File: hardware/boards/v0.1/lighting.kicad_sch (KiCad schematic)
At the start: 19 parts, among them U10 TRIG9, U11 TRIG13, U12 TRIG10, U13 TRIG14, U14 TRIG11, U15 TRIG15, U16 TRIG12, U17 TRIG16, U2 TRIG1, U3 TRIG2, U33 SN74AHCT1G125DBVR, U4 TRIG3, U5 TRIG4, U6 TRIG8, U7 TRIG7, U8 TRIG6, U9 TRIG5

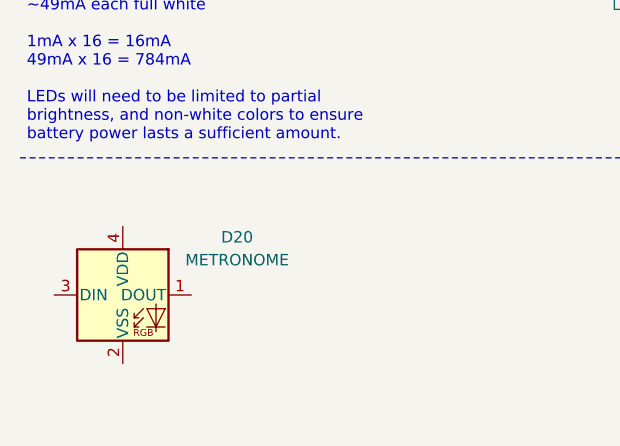
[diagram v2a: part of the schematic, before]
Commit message: feat: more routing and DRC cleanup
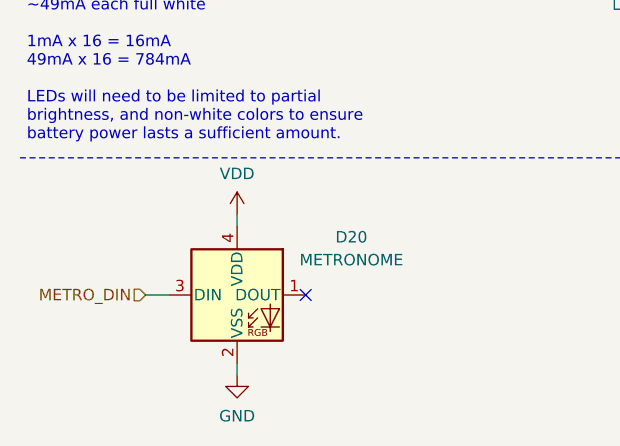
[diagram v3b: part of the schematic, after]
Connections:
- net GND: now also D20.2 (VSS)
- net VDD: now also D20.4 (VDD)
- net METRO_DIN: now reaches D20.3 (DIN)
- no-connect marks 1 -> 2
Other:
- moved on the sheet: D20
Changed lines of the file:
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@@
 	)
 	(no_connect
+		(at 44.45 181.61)
+	)
+	(no_connect
 		(at 69.85 138.43)
 	)
@@
 	(wire
 		(pts
+			(xy 26.67 181.61) (xy 29.21 181.61)
+		)
+		(stroke
+			(width 0)
+			(type default)
+		)
+	)
+	(wire
+		(pts
 			(xy 78.74 58.42) (xy 78.74 60.96)
 		)
@@
 	(wire
 		(pts
+			(xy 36.83 189.23) (xy 36.83 190.5)
+		)
+		(stroke
+			(width 0)
+			(type default)
+		)
+	)
+	(wire
+		(pts
 			(xy 129.54 114.3) (xy 129.54 116.84)
 		)
@@
 	(wire
 		(pts
+			(xy 36.83 172.72) (xy 36.83 173.99)
+		)
+		(stroke
+			(width 0)
+			(type default)
+		)
+	)
+	(wire
+		(pts
 			(xy 104.14 83.82) (xy 129.54 83.82)
 		)
@@
 		)
 	)
+	(hierarchical_label "METRO_DIN"
+		(shape input)
+		(at 26.67 181.61 180)
+		(effects
+			(font
+				(size 1.27 1.27)
+			)
+			(justify right)
+		)
+	)
 	(symbol
 		(lib_id "pocket_synth:SK6812MINI-E")
@@
 	)
 	(symbol
+		(lib_id "power:GND")
+		(at 36.83 190.5 0)
+		(mirror y)
+		(unit 1)
+		(exclude_from_sim no)
+		(in_bom yes)
+		(on_board yes)
+		(dnp no)
+		(property "Reference" "#PWR0114"
+			(at 36.83 196.85 0)
+			(effects
+				(font
+					(size 1.27 1.27)
+				)
+				(hide yes)
+			)
+		)
+		(property "Value" "GND"
+			(at 36.83 195.072 0)
+			(effects
+				(font
+					(size 1.27 1.27)
+				)
+			)
+		)
+		(property "Footprint" ""
+			(at 36.83 190.5 0)
+			(effects
+				(font
+					(size 1.27 1.27)
+				)
+				(hide yes)
+			)
+		)
+		(property "Datasheet" ""
+			(at 36.83 190.5 0)
+			(effects
+				(font
+					(size 1.27 1.27)
+				)
+				(hide yes)
+			)
+		)
+		(property "Description" "Power symbol creates a global label with name \"GND\" , ground"
+			(at 36.83 190.5 0)
+			(effects
+				(font
+					(size 1.27 1.27)
+				)
+				(hide yes)
+			)
+		)
+		(pin "1"
+		)
+		(instances
+			(project "pocket_synth"
+				(path "/485383b8-00f4-4405-b270-de249939cff4/ecdfb102-30c7-4f5a-8eb8-8f15fcbab9da"
+					(reference "#PWR0114")
+					(unit 1)
+				)
+			)
+		)
+	)
+	(symbol
 		(lib_id "pocket_synth:SK6812MINI-E")
 		(at 154.94 39.37 0)
@@
 	(symbol
 		(lib_id "LED:SK6812MINI")
-		(at 24.13 181.61 0)
+		(at 36.83 181.61 0)
 		(unit 1)
 		(exclude_from_sim no)
@@
 		(dnp no)
 		(property "Reference" "D20"
-			(at 36.83 175.1898 0)
+			(at 49.53 175.1898 0)
 			(effects
 				(font
@@
 		)
 		(property "Value" "METRONOME"
-			(at 36.83 177.7298 0)
+			(at 49.53 177.7298 0)
 			(effects
 				(font
@@
 		)
 		(property "Footprint" "LED_SMD:LED_SK6812MINI_PLCC4_3.5x3.5mm_P1.75mm"
-			(at 25.4 189.23 0)
+			(at 38.1 189.23 0)
 			(effects
 				(font
@@
 		)
 		(property "Datasheet" "https://cdn-shop.adafruit.com/product-files/2686/SK6812MINI_REV.01-1-2.pdf"
-			(at 26.67 191.135 0)
+			(at 39.37 191.135 0)
 			(effects
 				(font
@@
 		)
 		(property "Description" "RGB LED with integrated controller"
-			(at 24.13 181.61 0)
+			(at 36.83 181.61 0)
 			(effects
 				(font
@@
 		)
 		(property "Arrow Part Number" ""
-			(at 24.13 181.61 0)
+			(at 36.83 181.61 0)
 			(effects
 				(font
@@
 		)
 		(property "Arrow Price/Stock" ""
-			(at 24.13 181.61 0)
+			(at 36.83 181.61 0)
 			(effects
 				(font
@@
 		)
 		(property "MANUFACTURER" ""
-			(at 24.13 181.61 0)
+			(at 36.83 181.61 0)
 			(effects
 				(font
@@
 		)
 		(property "MAXIMUM_PACKAGE_HEIGHT" ""
-			(at 24.13 181.61 0)
+			(at 36.83 181.61 0)
 			(effects
 				(font
@@
 		)
 		(property "PARTREV" ""
-			(at 24.13 181.61 0)
+			(at 36.83 181.61 0)
 			(effects
 				(font
@@
 		)
 		(property "STANDARD" ""
-			(at 24.13 181.61 0)
+			(at 36.83 181.61 0)
 			(effects
 				(font
@@
 		)
 		(property "Connector" ""
-			(at 24.13 181.61 0)
+			(at 36.83 181.61 0)
 			(effects
 				(font
@@
 					(unit 1)
 				)
+			)
+		)
+	)
+	(symbol
+		(lib_id "power:VDD")
+		(at 36.83 172.72 0)
+		(mirror y)
+		(unit 1)
+		(exclude_from_sim no)
+		(in_bom yes)
+		(on_board yes)
+		(dnp no)
+		(property "Reference" "#PWR0113"
+			(at 36.83 176.53 0)
+			(effects
+				(font
+					(size 1.27 1.27)
+				)
+				(hide yes)
+			)
+		)
+		(property "Value" "VDD"
+			(at 36.83 168.148 0)
+			(effects
+				(font
+					(size 1.27 1.27)
+				)
+			)
+		)
+		(property "Footprint" ""
+			(at 36.83 172.72 0)
+			(effects
+				(font
+					(size 1.27 1.27)
+				)
+				(hide yes)
+			)
+		)
+		(property "Datasheet" ""
+			(at 36.83 172.72 0)
+			(effects
+				(font
+					(size 1.27 1.27)
+				)
+				(hide yes)
+			)
+		)
+		(property "Description" "Power symbol creates a global label with name \"VDD\""
+			(at 36.83 172.72 0)
+			(effects
+				(font
+					(size 1.27 1.27)
+				)
+				(hide yes)
+			)
+		)
+		(pin "1"
+		)
+		(instances
+			(project "pocket_synth"
+				(path "/485383b8-00f4-4405-b270-de249939cff4/ecdfb102-30c7-4f5a-8eb8-8f15fcbab9da"
+					(reference "#PWR0113")
+					(unit 1)
+				)

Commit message: feat: clean up routing, remove metronome light
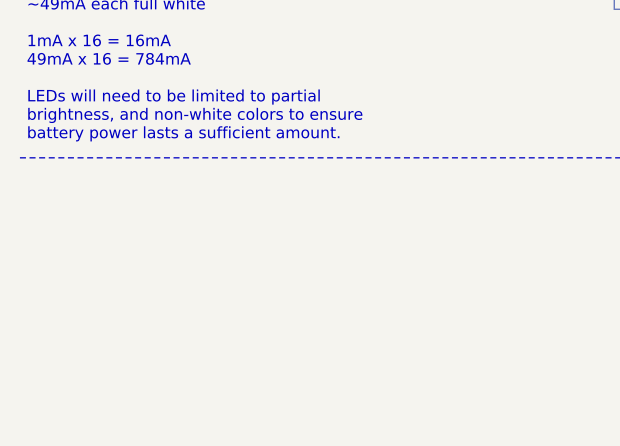
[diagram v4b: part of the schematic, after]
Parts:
- removed D20: METRONOME, LED_SMD:LED_SK6812MINI_PLCC4_3.5x3.5mm_P1.75mm, symbol LED:SK6812MINI
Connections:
- no-connect marks 2 -> 1

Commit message: feat: routing cleanup and start of BOM selection
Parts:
- R35: JLC (none) -> C25531
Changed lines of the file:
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@@
+			)
+		)
+		(property "JLC" "C25531"
+			(at 29.21 45.72 0)
+			(effects
+				(font
+					(size 1.27 1.27)
+				)
+				(hide yes)
 			)
 		)

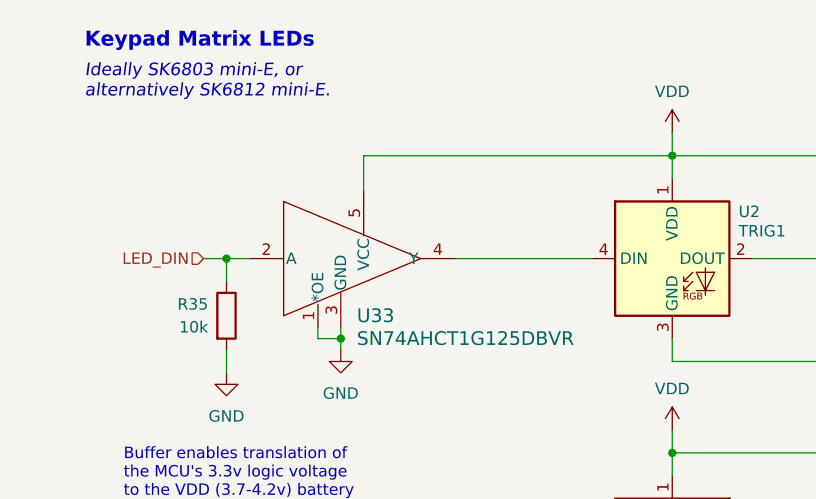
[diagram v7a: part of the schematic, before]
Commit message: feat: swap out of stock components
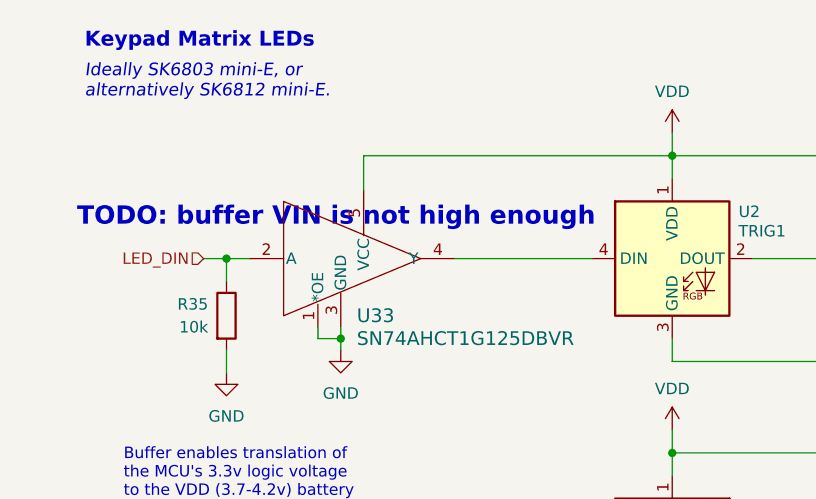
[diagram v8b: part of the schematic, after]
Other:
- note added: "TODO: buffer VIN is not high enough"
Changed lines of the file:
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@@
+		)
+	)
+	(text "TODO: buffer VIN is not high enough"
+		(exclude_from_sim no)
+		(at 41.402 34.798 0)
+		(effects
+			(font
+				(size 2.032 2.032)
+				(thickness 0.4064)
+				(bold yes)
+				(color 194 0 0 1)
+			)
 		)
 	)
